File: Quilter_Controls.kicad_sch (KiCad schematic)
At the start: 19 parts, among them J1 Conn_01x10_Male, J10 Conn_01x04_Male, J11 Freq_In, J2 Conn_01x10_Male, J3 Conn_01x10_Male, J4 Audio_In, J5 Audio_Out, J6 Audio_Mix, J7 Freq_V_Oct, J8 Freq_CV, J9 Conn_02x04_Top_Bottom

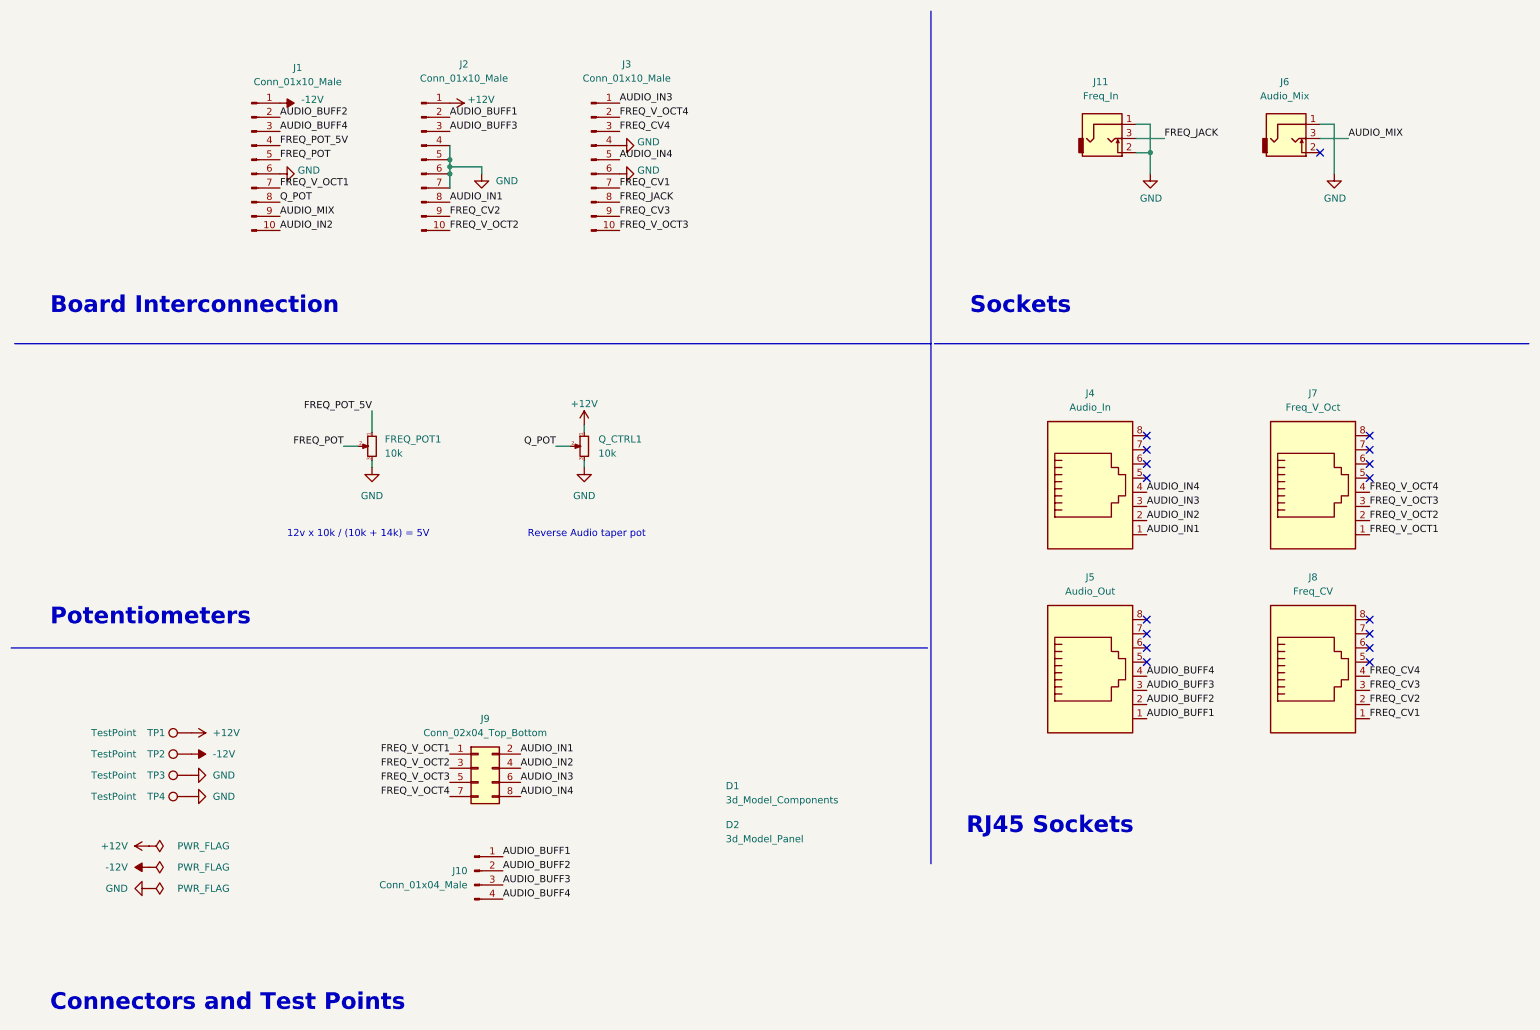
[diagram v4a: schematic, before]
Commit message: Cleaned up panel and PCBs
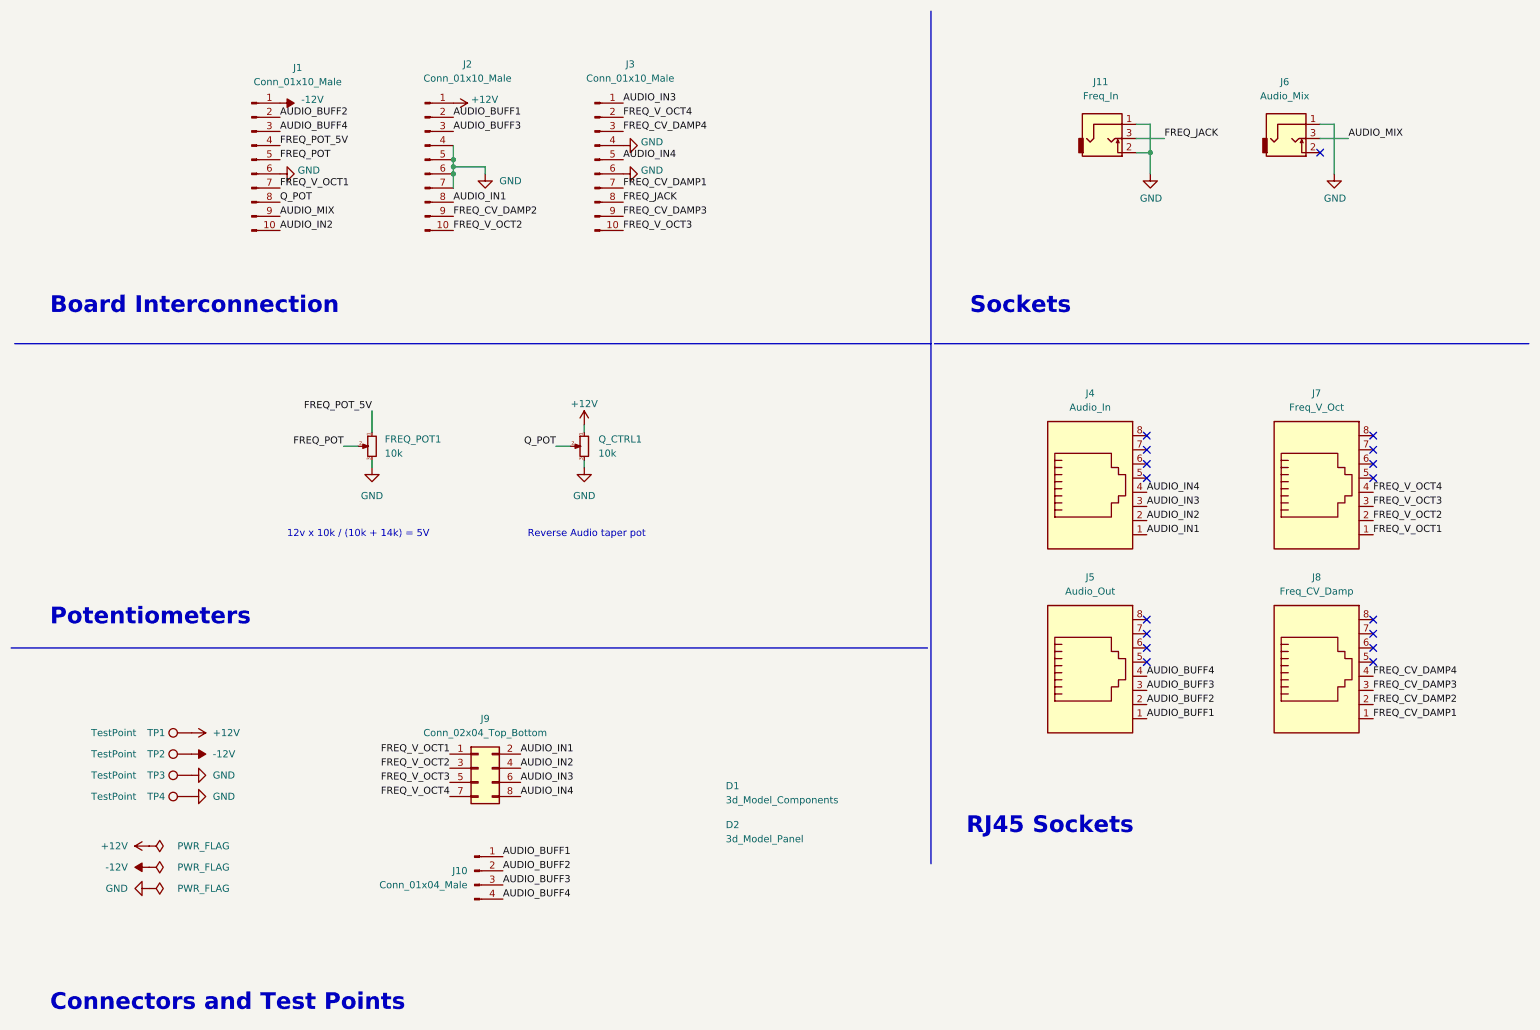
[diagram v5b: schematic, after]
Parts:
- J8: value Freq_CV -> Freq_CV_Damp
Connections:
- net FREQ_CV1 renamed FREQ_CV_DAMP1
- net FREQ_CV2 renamed FREQ_CV_DAMP2
- net FREQ_CV3 renamed FREQ_CV_DAMP3
- net FREQ_CV4 renamed FREQ_CV_DAMP4
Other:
- moved on the sheet: J2, J3, J7, J8

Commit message: Added Readme and revision notes
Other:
- company: (none) -> Mountjoy Modular
- title: (none) -> Quilter Controls
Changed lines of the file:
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@@
 (kicad_sch (version 20211123) (generator eeschema)
   (paper "A4")
+  (title_block
+    (title "Quilter Controls")
+    (date "2023-03-22")
+    (rev "v1.0")
+    (company "Mountjoy Modular")
+  )
   (junction (at 91.44 41.91) (diameter 0) (color 0 0 0 0)
   )

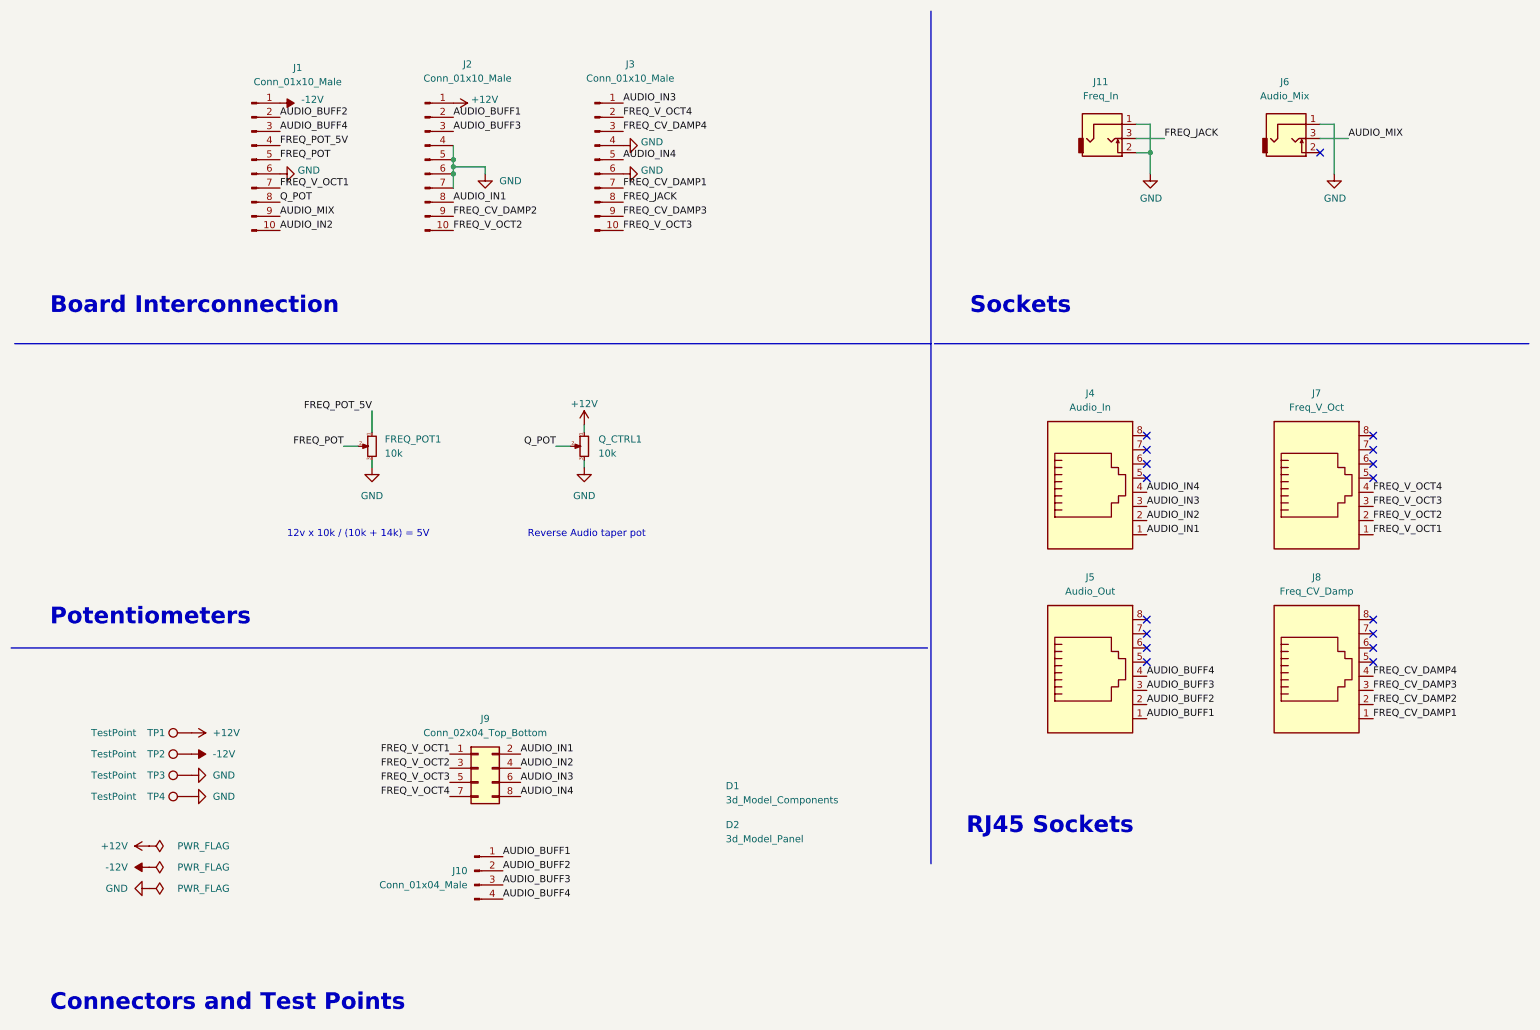
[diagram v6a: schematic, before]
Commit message: Updates for v2, including dc blocking caps on output
Also adjusted lower range of cutoff knob and tweaked various resistor values
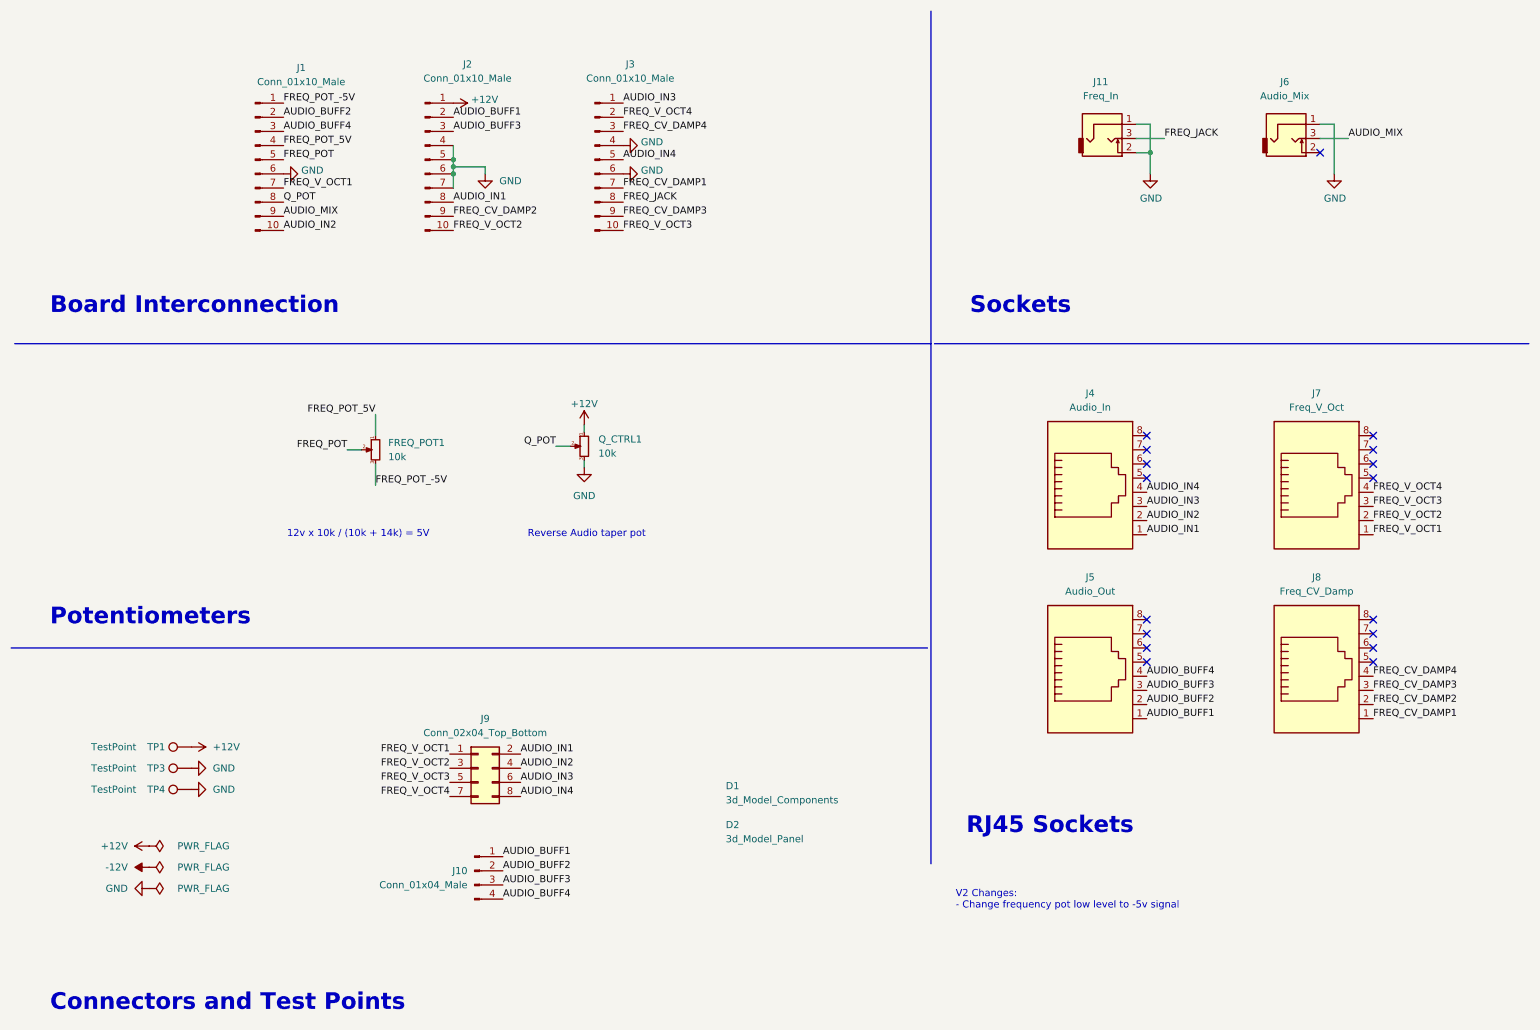
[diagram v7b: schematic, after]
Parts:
- removed TP2: TestPoint, Custom_Footprints:1.3mm_Test_Point, symbol Connector:TestPoint
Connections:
- net -12V: no longer J1.1 (Pin_1)
- net GND: no longer FREQ_POT1.3
- new net FREQ_POT_-5V: FREQ_POT1.3, J1.1 (Pin_1)
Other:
- note added: "V2 Changes: - Change frequency pot low level to -5v signal"
- moved on the sheet: FREQ_POT1, J1, TP1, TP3, TP4
